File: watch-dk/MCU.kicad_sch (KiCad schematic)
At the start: 41 parts, among them IC601 FAN5622SX, IC602 USBLC6-2P6, IC603 MX25U51245GZ4I00, IC604 NTS0104GU12, J601 Jumper, J602 Jumper, J603 Jumper, J604 Jumper, M601 NORA-B106, X601 DEBUG, X602 Current, X603 Device, X604 UART, X605 GPIO, X606 Current, X607 IO Current, X608 Display, X609 Touch Current, X610 LED Current

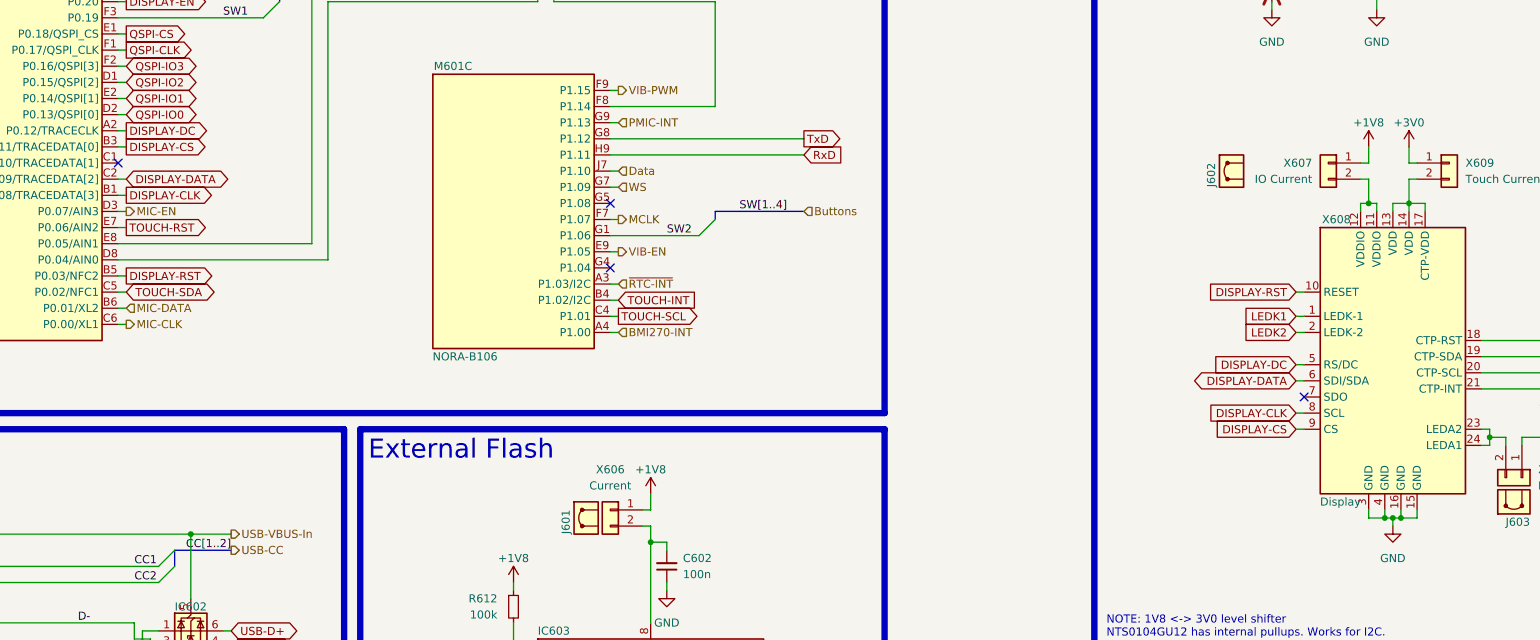
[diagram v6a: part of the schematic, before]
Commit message: Feature: Issue #145
- Update symbols

Signed-off-by: Daniel Kampert <DanielKampert@kampis-elektroecke.de>
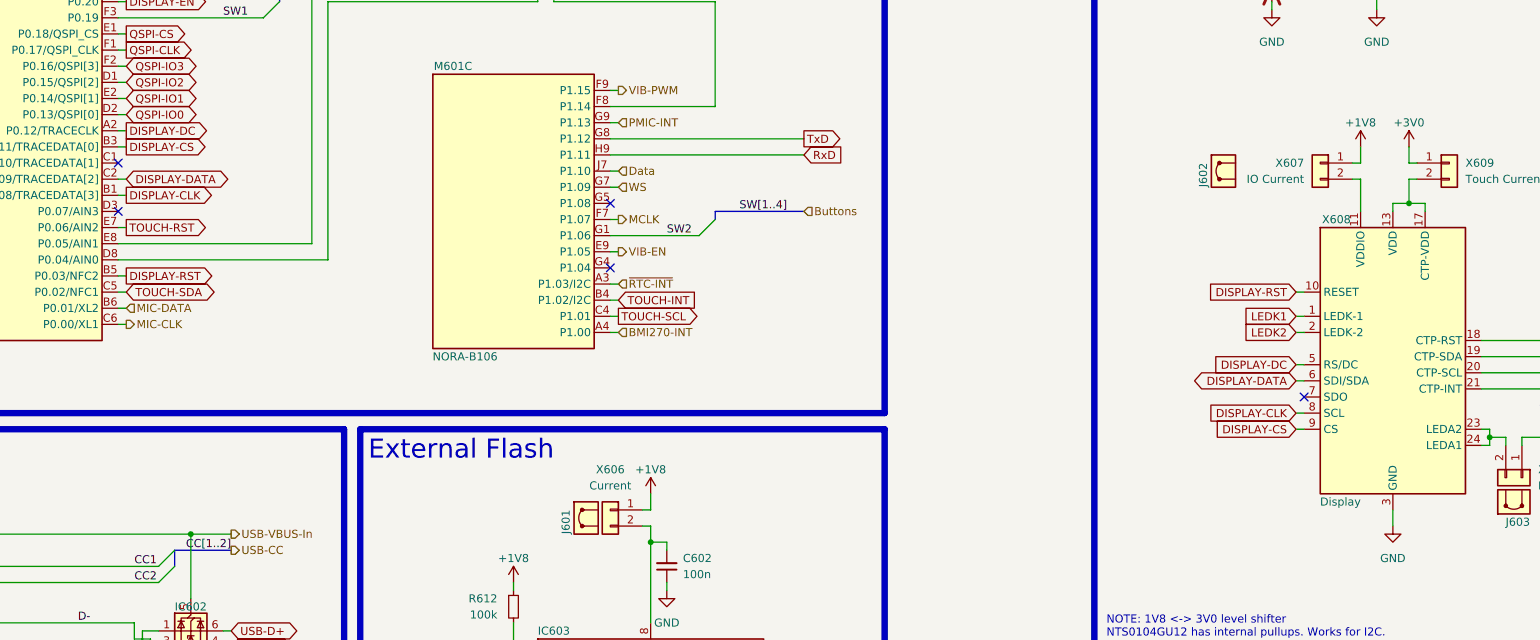
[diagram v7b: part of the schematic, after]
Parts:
- IC601: symbol ON Semiconductor:FAN5622SX -> ON Semiconductor:FAN5622
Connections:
- net MIC-EN: no longer names the net of M601.D3 (P0.07/AIN3)
- no-connect marks 11 -> 12
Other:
- moved on the sheet: J602, X607
